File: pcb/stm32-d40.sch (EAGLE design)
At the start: 33 parts, among them IC1 TODO AMIS30663CANG2G, IC2 STM32F103C8, J1 DIP-40, Q2 8MHz, SW1 KSS-2EG4430, SW2 KSS-2EG4430, X1 DG3XX-03-3.5

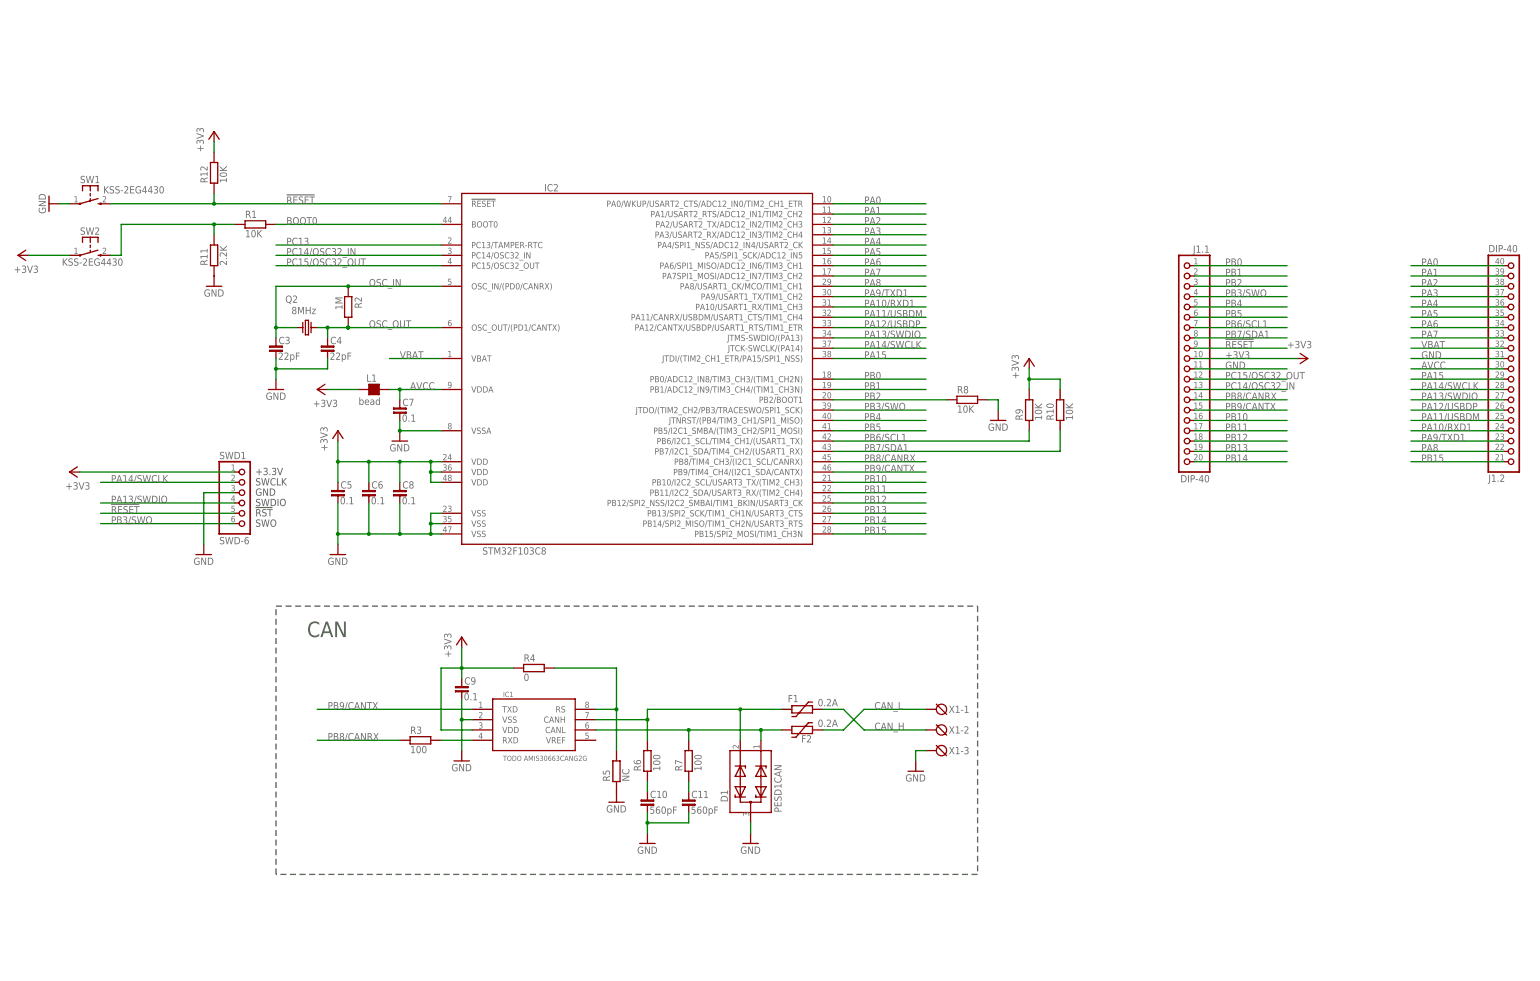
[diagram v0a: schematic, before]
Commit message: DIP40 CAN ready
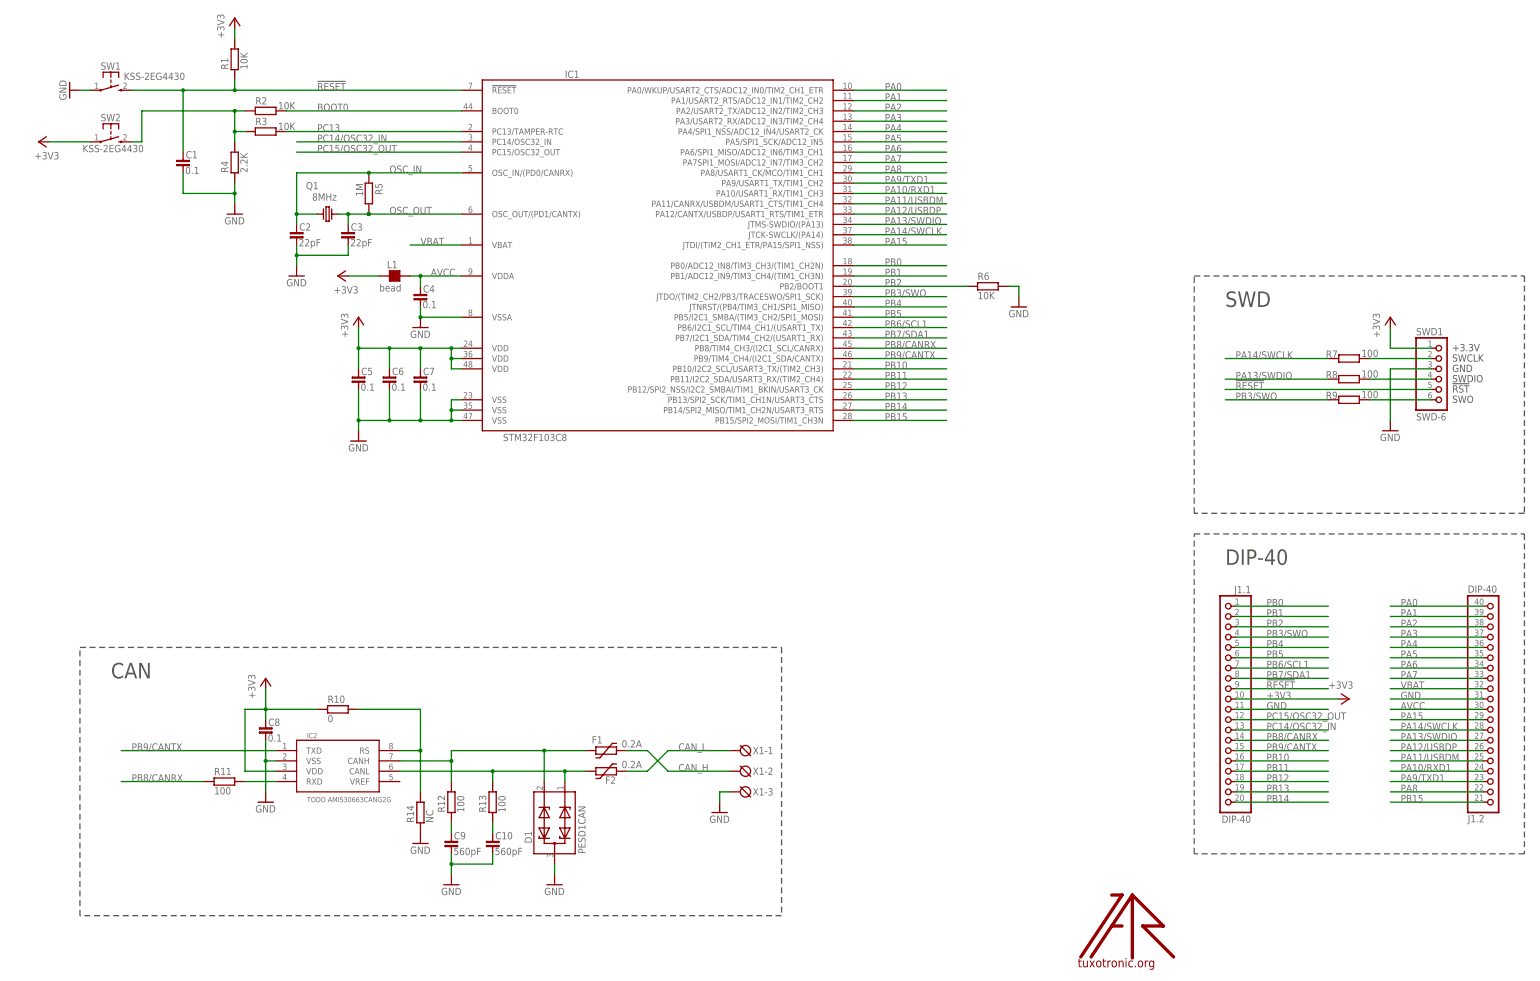
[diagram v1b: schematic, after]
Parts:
- removed C11: 560pF, rc-master-smd:C_0603
- removed Q2: 8MHz, discrete:CRYSTAL-HC49S
- added C1: 0.1, rc-master-smd:C_0603
- added C2: 22pF, rc-master-smd:C_0603
- added Q1: 8MHz, discrete:CRYSTAL-HC49S
- added R13: 100, rc-master-smd:R_0603
- added R14: NC, rc-master-smd:R_0603
- added U$: LOGO, logo:LOGO
- C4: value 22pF -> 0.1
- C9: value 0.1 -> 560pF
- IC1: value TODO AMIS30663CANG2G -> STM32F103C8; device interfaces:SN65HVD230 -> stm32:STM32F103C8
- IC2: value STM32F103C8 -> TODO AMIS30663CANG2G; device stm32:STM32F103C8 -> interfaces:SN65HVD230
- R10: value 10K -> 0
- R11: value 2.2K -> 100
- R12, R8, R9: value 10K -> 100
- R2: value 1M -> 10K
- R3, R6: value 100 -> 10K
- R4: value 0 -> 2.2K
- R5: value NC -> 1M
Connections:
- new net N$2: R7.2, SWD1.2
- new net N$3: R8.2, SWD1.4
- new net N$4: R9.2, SWD1.6
- net !RESET: now also C1.1, IC1.!RESET, R1.1; no longer IC2.!RESET, R12.1
- net +3V3: now also C7.1, IC1.VDD@1, IC1.VDD@2, IC1.VDD@3, IC2.VDD, R1.2, R10.1; no longer C9.1, IC1.VDD, IC2.VDD@1, IC2.VDD@2, IC2.VDD@3, R10.2, R12.2, R4.1, R9.2
- net AVCC: now also C4.1, IC1.VDDA; no longer C7.1, IC2.VDDA
- net BOOT0: now also IC1.BOOT0, R2.2; no longer IC2.BOOT0, R1.2
- net CAN_CTRL: now also IC2.RS, R10.2, R14.2; no longer IC1.RS, R4.2, R5.2
- net GND: now also C1.2, C2.2, IC1.VSS@1, IC1.VSS@2, IC1.VSS@3, IC1.VSSA, IC2.VSS, R14.1, R4.1, R6.2; no longer C11.2, IC1.VSS, IC2.VSS@1, IC2.VSS@2, IC2.VSS@3, IC2.VSSA, R11.1, R5.1, R8.2
- net N$1: now also R2.1, R3.1, R4.2; no longer R1.1, R11.2
- net N$51: now also IC2.CANH, R12.2; no longer IC1.CANH, R6.2
- net N$52: now also IC2.CANL, R13.2; no longer IC1.CANL, R7.2
- net N$54: now also C10.1, R13.1; no longer C11.1, R7.1
- net N$55: now also C9.1, R12.1; no longer C10.1, R6.1
- net N$7: now also IC2.RXD, R11.2; no longer IC1.RXD, R3.2
- net OSC_IN: now also C2.1, IC1.OSC_IN/(PD0/CANRX), Q1.1, R5.1; no longer C3.1, IC2.OSC_IN/(PD0/CANRX), Q2.1, R2.1
- net OSC_OUT: now also C3.1, IC1.OSC_OUT/(PD1/CANTX), Q1.2, R5.2; no longer C4.1, IC2.OSC_OUT/(PD1/CANTX), Q2.2, R2.2
- net PA0: now also IC1.PA0/WKUP/USART2_CTS/ADC12_IN0/TIM2_CH1_ETR; no longer IC2.PA0/WKUP/USART2_CTS/ADC12_IN0/TIM2_CH1_ETR
- net PA1: now also IC1.PA1/USART2_RTS/ADC12_IN1/TIM2_CH2; no longer IC2.PA1/USART2_RTS/ADC12_IN1/TIM2_CH2
- net PA10/RXD1: now also IC1.PA10/USART1_RX/TIM1_CH3; no longer IC2.PA10/USART1_RX/TIM1_CH3
- net PA11/USBDM: now also IC1.PA11/CANRX/USBDM/USART1_CTS/TIM1_CH4; no longer IC2.PA11/CANRX/USBDM/USART1_CTS/TIM1_CH4
- net PA12/USBDP: now also IC1.PA12/CANTX/USBDP/USART1_RTS/TIM1_ETR; no longer IC2.PA12/CANTX/USBDP/USART1_RTS/TIM1_ETR
- net PA13/SWDIO: now also IC1.JTMS-SWDIO/(PA13), R8.1; no longer IC2.JTMS-SWDIO/(PA13), SWD1.4
- net PA14/SWCLK: now also IC1.JTCK-SWCLK/(PA14), R7.1; no longer IC2.JTCK-SWCLK/(PA14), SWD1.2
- net PA15: now also IC1.JTDI/(TIM2_CH1_ETR/PA15/SPI1_NSS); no longer IC2.JTDI/(TIM2_CH1_ETR/PA15/SPI1_NSS)
- net PA2: now also IC1.PA2/USART2_TX/ADC12_IN2/TIM2_CH3; no longer IC2.PA2/USART2_TX/ADC12_IN2/TIM2_CH3
- net PA3: now also IC1.PA3/USART2_RX/ADC12_IN3/TIM2_CH4; no longer IC2.PA3/USART2_RX/ADC12_IN3/TIM2_CH4
- net PA4: now also IC1.PA4/SPI1_NSS/ADC12_IN4/USART2_CK; no longer IC2.PA4/SPI1_NSS/ADC12_IN4/USART2_CK
- net PA5: now also IC1.PA5/SPI1_SCK/ADC12_IN5; no longer IC2.PA5/SPI1_SCK/ADC12_IN5
- net PA6: now also IC1.PA6/SPI1_MISO/ADC12_IN6/TIM3_CH1; no longer IC2.PA6/SPI1_MISO/ADC12_IN6/TIM3_CH1
- net PA7: now also IC1.PA7SPI1_MOSI/ADC12_IN7/TIM3_CH2; no longer IC2.PA7SPI1_MOSI/ADC12_IN7/TIM3_CH2
- net PA8: now also IC1.PA8/USART1_CK/MCO/TIM1_CH1; no longer IC2.PA8/USART1_CK/MCO/TIM1_CH1
- net PA9/TXD1: now also IC1.PA9/USART1_TX/TIM1_CH2; no longer IC2.PA9/USART1_TX/TIM1_CH2
- net PB0: now also IC1.PB0/ADC12_IN8/TIM3_CH3/(TIM1_CH2N); no longer IC2.PB0/ADC12_IN8/TIM3_CH3/(TIM1_CH2N)
- net PB1: now also IC1.PB1/ADC12_IN9/TIM3_CH4/(TIM1_CH3N); no longer IC2.PB1/ADC12_IN9/TIM3_CH4/(TIM1_CH3N)
- net PB10: now also IC1.PB10/I2C2_SCL/USART3_TX/(TIM2_CH3); no longer IC2.PB10/I2C2_SCL/USART3_TX/(TIM2_CH3)
- net PB11: now also IC1.PB11/I2C2_SDA/USART3_RX/(TIM2_CH4); no longer IC2.PB11/I2C2_SDA/USART3_RX/(TIM2_CH4)
- net PB12: now also IC1.PB12/SPI2_NSS/I2C2_SMBAI/TIM1_BKIN/USART3_CK; no longer IC2.PB12/SPI2_NSS/I2C2_SMBAI/TIM1_BKIN/USART3_CK
- net PB13: now also IC1.PB13/SPI2_SCK/TIM1_CH1N/USART3_CTS; no longer IC2.PB13/SPI2_SCK/TIM1_CH1N/USART3_CTS
- net PB14: now also IC1.PB14/SPI2_MISO/TIM1_CH2N/USART3_RTS; no longer IC2.PB14/SPI2_MISO/TIM1_CH2N/USART3_RTS
- net PB15: now also IC1.PB15/SPI2_MOSI/TIM1_CH3N; no longer IC2.PB15/SPI2_MOSI/TIM1_CH3N
- net PB2: now also IC1.PB2/BOOT1, R6.1; no longer IC2.PB2/BOOT1, R8.1
- net PB3/SWO: now also IC1.JTDO/(TIM2_CH2/PB3/TRACESWO/SPI1_SCK), R9.1; no longer IC2.JTDO/(TIM2_CH2/PB3/TRACESWO/SPI1_SCK), SWD1.6
- net PB4: now also IC1.JTNRST/(PB4/TIM3_CH1/SPI1_MISO); no longer IC2.JTNRST/(PB4/TIM3_CH1/SPI1_MISO)
- net PB5: now also IC1.PB5/I2C1_SMBA/(TIM3_CH2/SPI1_MOSI); no longer IC2.PB5/I2C1_SMBA/(TIM3_CH2/SPI1_MOSI)
- net PB6/SCL1: now also IC1.PB6/I2C1_SCL/TIM4_CH1/(USART1_TX); no longer IC2.PB6/I2C1_SCL/TIM4_CH1/(USART1_TX), R9.1
- net PB7/SDA1: now also IC1.PB7/I2C1_SDA/TIM4_CH2/(USART1_RX); no longer IC2.PB7/I2C1_SDA/TIM4_CH2/(USART1_RX), R10.1
- net PB8/CANRX: now also IC1.PB8/TIM4_CH3/(I2C1_SCL/CANRX), R11.1; no longer IC2.PB8/TIM4_CH3/(I2C1_SCL/CANRX), R3.1
- net PB9/CANTX: now also IC1.PB9/TIM4_CH4/(I2C1_SDA/CANTX), IC2.TXD; no longer IC1.TXD, IC2.PB9/TIM4_CH4/(I2C1_SDA/CANTX)
- net PC13: now also IC1.PC13/TAMPER-RTC, R3.2; no longer IC2.PC13/TAMPER-RTC
- net PC14/OSC32_IN: now also IC1.PC14/OSC32_IN; no longer IC2.PC14/OSC32_IN
- net PC15/OSC32_OUT: now also IC1.PC15/OSC32_OUT; no longer IC2.PC15/OSC32_OUT
- net VBAT: now also IC1.VBAT; no longer IC2.VBAT
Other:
- note added: "DIP-40"
- note added: "SWD"
- moved on the sheet: C10, C3, C4, C5, C6, C7, C8, C9, D1, F1, F2, J1.1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

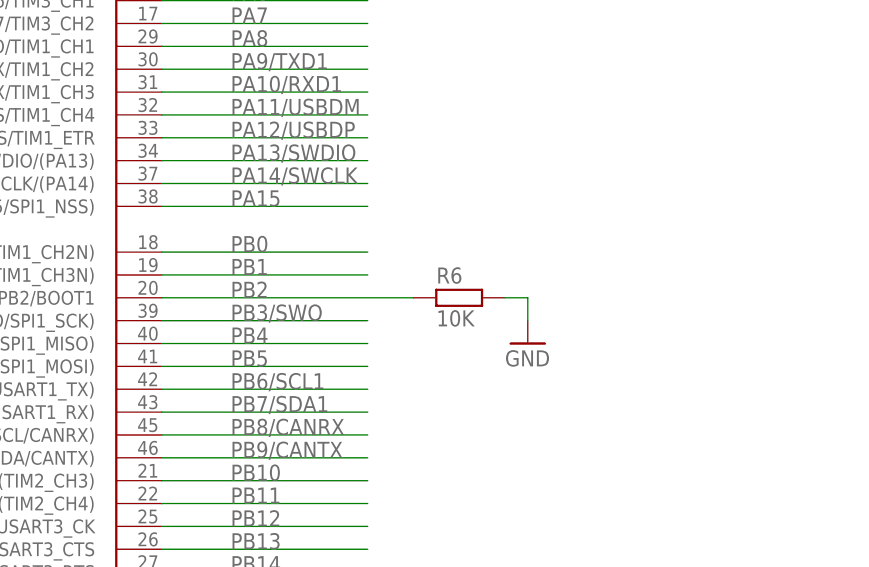
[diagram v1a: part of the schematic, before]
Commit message: some wire fixes, add LED
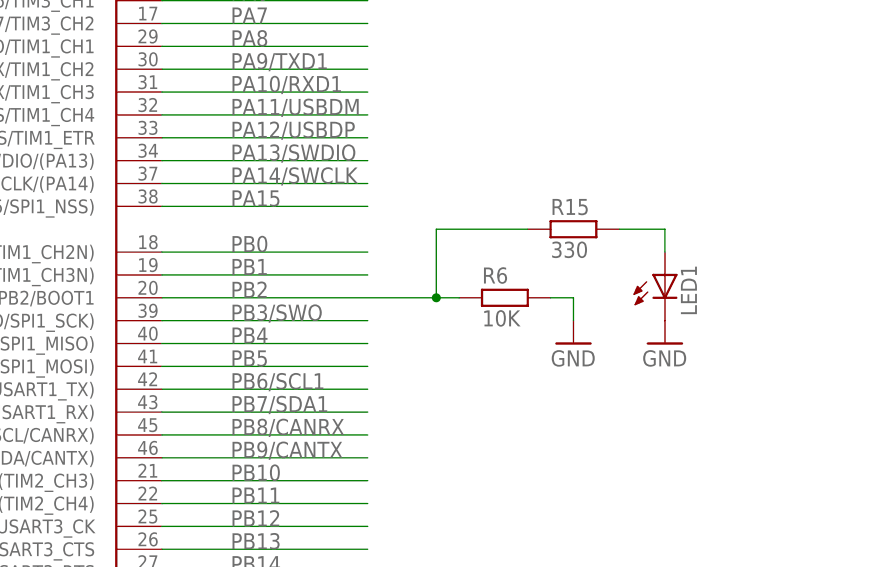
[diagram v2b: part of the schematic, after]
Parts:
- added LED1: (no value), led:LEDCHIPLED_0603
- added R15: 330, rc-master-smd:R_0603
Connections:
- new net N$5: LED1.A, R15.2
- net GND: now also LED1.C
- net PB2: now also R15.1
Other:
- moved on the sheet: R6
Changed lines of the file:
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@@
 <part name="R8" library="rc-master-smd" deviceset="R_" device="0603" value="100"/>
 <part name="R9" library="rc-master-smd" deviceset="R_" device="0603" value="100"/>
+<part name="LED1" library="led" deviceset="LED" device="CHIPLED_0603"/>
+<part name="GND6" library="rs485" deviceset="GND" device=""/>
+<part name="R15" library="rc-master-smd" deviceset="R_" device="0603" value="330"/>
 </parts>
 <sheets>
@@
 <instance part="X1" gate="-2" x="175.26" y="48.26"/>
 <instance part="X1" gate="-3" x="175.26" y="43.18"/>
-<instance part="R6" gate="G$1" x="236.22" y="167.64"/>
-<instance part="GND2" gate="1" x="243.84" y="162.56"/>
+<instance part="R6" gate="G$1" x="241.3" y="167.64"/>
+<instance part="GND2" gate="1" x="248.92" y="162.56"/>
 <instance part="IC2" gate="G$1" x="76.2" y="50.8"/>
 <instance part="+3V19" gate="G$1" x="58.42" y="71.12"/>
@@
 <attribute name="VALUE" x="328.168" y="140.081" size="1.778" layer="96"/>
 </instance>
+<instance part="LED1" gate="G$1" x="259.08" y="170.18"/>
+<instance part="GND6" gate="1" x="259.08" y="162.56"/>
+<instance part="R15" gate="G$1" x="248.92" y="175.26"/>
 </instances>
 <busses>
@@
 <pinref part="R6" gate="G$1" pin="2"/>
 <pinref part="GND2" gate="1" pin="GND"/>
-<wire x1="241.3" y1="167.64" x2="243.84" y2="167.64" width="0.1524" layer="91"/>
-<wire x1="243.84" y1="167.64" x2="243.84" y2="165.1" width="0.1524" layer="91"/>
+<wire x1="246.38" y1="167.64" x2="248.92" y2="167.64" width="0.1524" layer="91"/>
+<wire x1="248.92" y1="167.64" x2="248.92" y2="165.1" width="0.1524" layer="91"/>
 </segment>
 <segment>
@@
 <wire x1="12.7" y1="215.9" x2="15.24" y2="215.9" width="0.1524" layer="91"/>
 </segment>
+<segment>
+<pinref part="LED1" gate="G$1" pin="C"/>
+<pinref part="GND6" gate="1" pin="GND"/>
+</segment>
 </net>
 <net name="PB2" class="0">
 <segment>
-<wire x1="203.2" y1="167.64" x2="231.14" y2="167.64" width="0.1524" layer="91"/>
+<wire x1="203.2" y1="167.64" x2="233.68" y2="167.64" width="0.1524" layer="91"/>
 <label x="210.82" y="167.64" size="1.778" layer="95"/>
 <pinref part="IC1" gate="G$1" pin="PB2/BOOT1"/>
 <pinref part="R6" gate="G$1" pin="1"/>
+<pinref part="R15" gate="G$1" pin="1"/>
+<wire x1="233.68" y1="167.64" x2="236.22" y2="167.64" width="0.1524" layer="91"/>
+<wire x1="243.84" y1="175.26" x2="233.68" y2="175.26" width="0.1524" layer="91"/>
+<wire x1="233.68" y1="175.26" x2="233.68" y2="167.64" width="0.1524" layer="91"/>
+<junction x="233.68" y="167.64"/>
 </segment>
 <segment>
@@
 </segment>
 </net>
+<net name="N$5" class="0">
+<segment>
+<pinref part="R15" gate="G$1" pin="2"/>
+<pinref part="LED1" gate="G$1" pin="A"/>
+<wire x1="254" y1="175.26" x2="259.08" y2="175.26" width="0.1524" layer="91"/>
+<wire x1="259.08" y1="175.26" x2="259.08" y2="172.72" width="0.1524" layer="91"/>
+</segment>
+</net>
